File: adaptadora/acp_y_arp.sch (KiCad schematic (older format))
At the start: 39 parts, among them J12 Conn_Coaxial, J13 Conn_Coaxial, J14 Conn_Coaxial, J15 Conn_Coaxial, J16 Conn_Coaxial, J17 Conn_Coaxial, U11 LM361MX_NOPB, U12 LM361MX_NOPB, U21 TLV2772IDR, U22 TLV2772IDR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

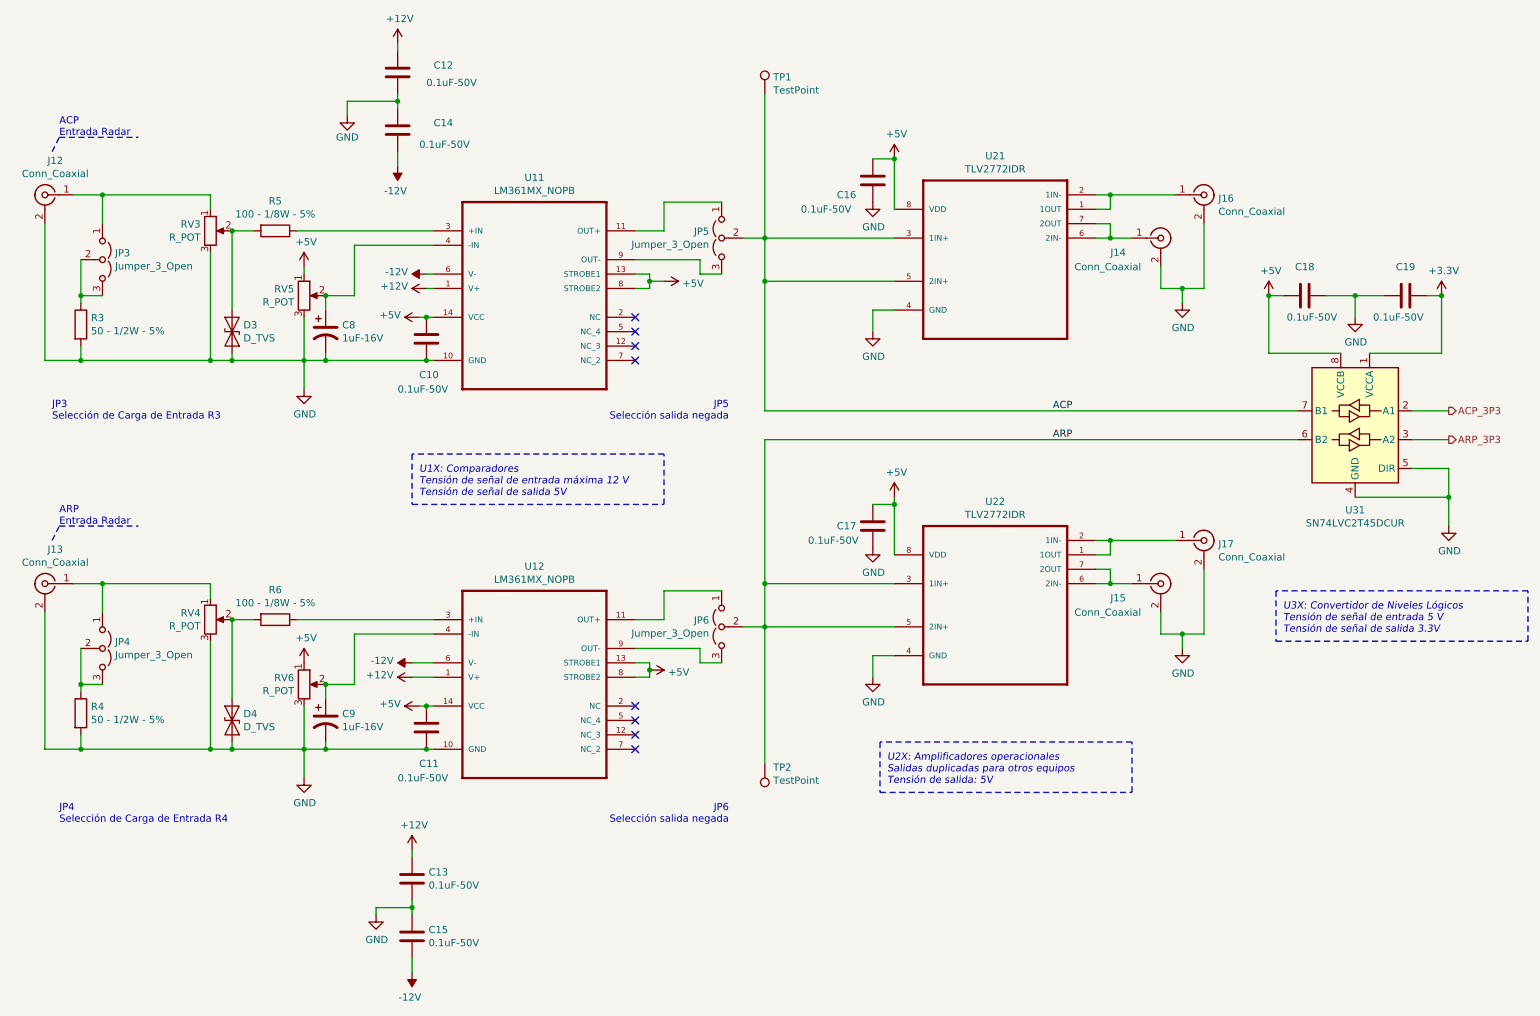
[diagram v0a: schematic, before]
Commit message: se ordenan campos de integrados
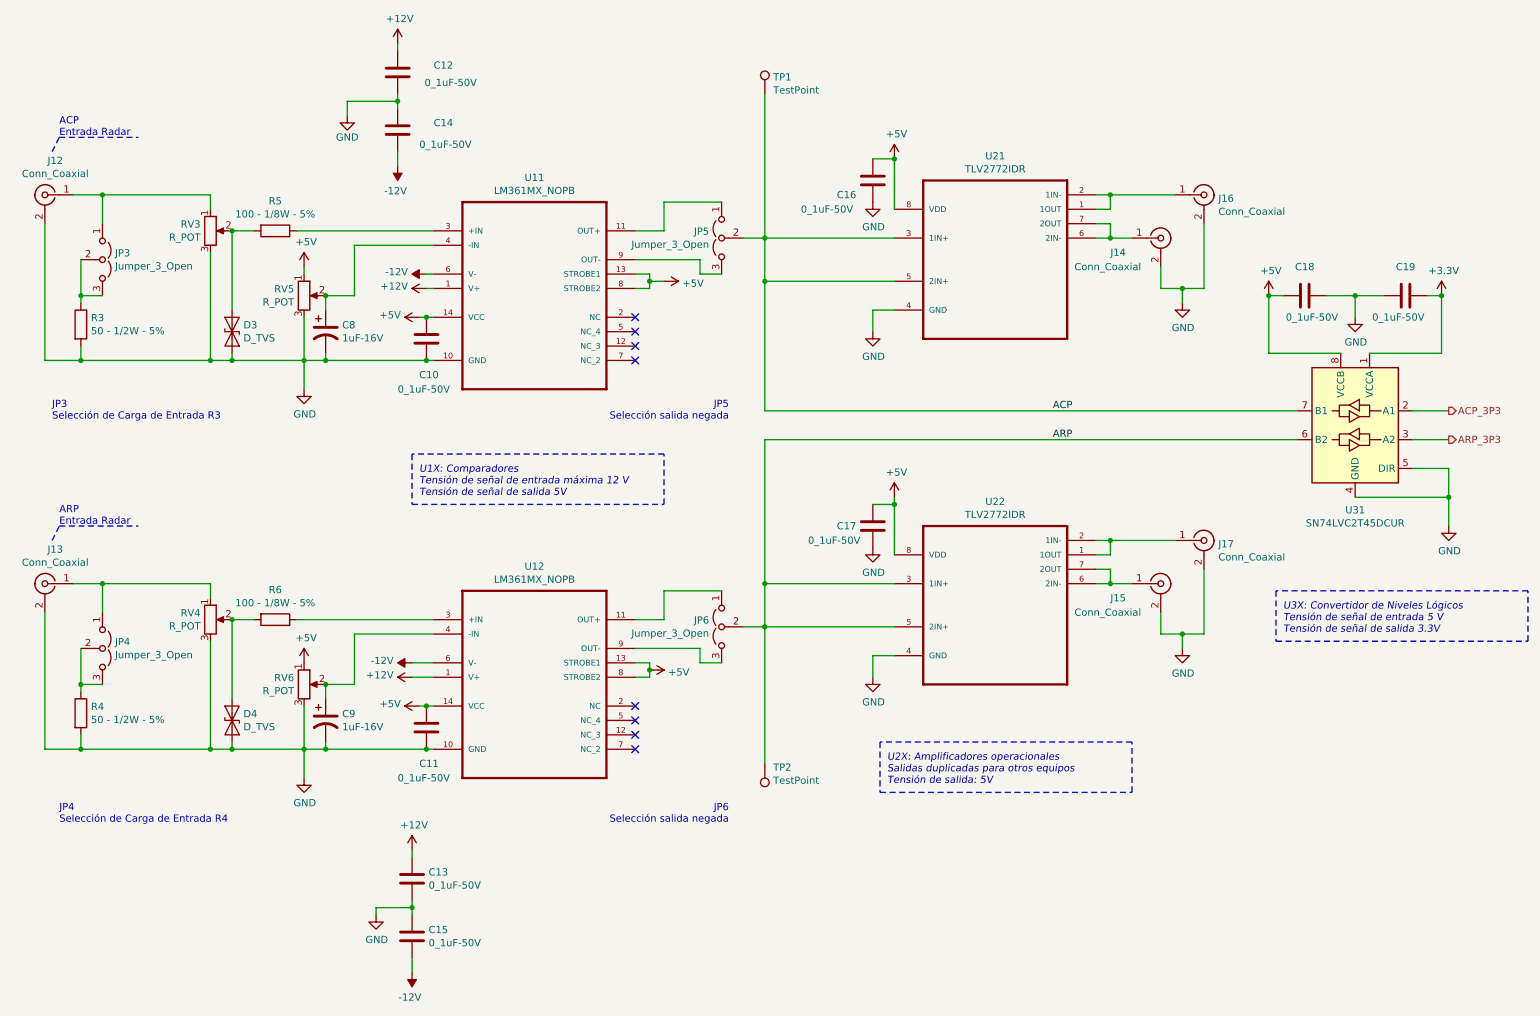
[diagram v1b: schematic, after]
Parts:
- C10, C11, C12, C13, C14, C15, C16, C17, C18, C19: value 0.1uF-50V -> 0_1uF-50V
- U11, U12: Número de parte (Digi-Key) 296-47682-1-ND -> (none)
- U21, U22: Descripción (inglés) General Purpose Amplifier 2 Circuit Rail-to-Rail 8-SOIC -> Dual 2.7-V High Slew Rate Rail-To-Rail Output Operational A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; Número de parte (Digi-Key) 296-1902-2-ND -> (none)
- U31: Número de parte (Digi-Key) 296-17014-1-ND -> (none)
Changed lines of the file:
@@
 P 3350 2950
 F 0 "C10" H 3400 3200 50  0000 R CNN
-F 1 "0.1uF-50V" H 3550 3300 50  0000 R CNN
+F 1 "0_1uF-50V" H 3550 3300 50  0000 R CNN
 F 2 "Capacitor_SMD:C_0805_2012Metric" H 3388 2800 50  0001 C CNN
 F 3 "~" H 3350 2950 50  0001 C CNN
@@
 F 4 "Texas Instruments" H 4100 2500 50  0001 L BNN "Fabricante"
 F 5 "High Speed Differential Comparator 14-SOIC 0 to 70" H 4100 2500 50  0001 L BNN "Descripción (inglés)"
-F 6 "296-47682-1-ND" H 4100 2500 50  0001 L BNN "Número de parte (Digi-Key)"
+F 6 "296-47682-1-ND" H 4100 2500 50  0001 L BNN "Número de Parte (Digi-Key)"
 F 7 "https://www.digikey.com/product-detail/en/texas-instruments/LM361MX-NOPB/296-47682-1-ND/3526971" H 4100 2500 50  0001 L BNN "Enlace"
-F 8 "296-47682-1-ND" H 4100 2500 50  0001 C CNN "Número de Parte (Digi-Key)"
 	1    4100 2500
 	1    0    0    -1
@@
 P 3150 1100
 F 0 "C12" H 2900 1150 50  0000 R CNN
-F 1 "0.1uF-50V" H 2600 1000 50  0000 L BNN
+F 1 "0_1uF-50V" H 2600 1000 50  0000 L BNN
 F 2 "Capacitor_SMD:C_0805_2012Metric" H 3188 950 50  0001 C CNN
 F 3 "~" H 3150 1100 50  0001 C CNN
@@
 P 3150 1500
 F 0 "C14" H 3400 1550 50  0000 L CNN
-F 1 "0.1uF-50V" H 3300 1400 50  0000 L CNN
+F 1 "0_1uF-50V" H 3300 1400 50  0000 L CNN
 F 2 "Capacitor_SMD:C_0805_2012Metric" H 3188 1350 50  0001 C CNN
 F 3 "~" H 3150 1500 50  0001 C CNN
@@
 F 3 "http://www.ti.com/lit/ds/symlink/tlv2772.pdf" H 7300 2250 50  0001 L BNN
 F 4 "Texas Instruments" H 7300 2250 50  0001 L BNN "Fabricante"
-F 5 "General Purpose Amplifier 2 Circuit Rail-to-Rail 8-SOIC" H 7300 2250 50  0001 L BNN "Descripción (inglés)"
+F 5 "Dual 2.7-V High Slew Rate Rail-To-Rail Output Operational Amplifier 8-SOIC -40 to 125" H 7300 2250 50  0001 L BNN "Descripción (inglés)"
 F 6 "296-1902-2-ND" H 7300 2250 50  0001 L BNN "Número de Parte (Digi-Key)"
 F 7 "https://www.digikey.com/product-detail/en/texas-instruments/TLV2772IDR/296-1902-2-ND/374332" H 7300 2250 50  0001 L BNN "Enlace"
-F 8 "296-1902-2-ND" H 7300 2250 50  0001 C CNN "Número de parte (Digi-Key)"
 	1    7300 2250
 	1    0    0    -1
@@
 P 10150 2650
 F 0 "C19" V 9950 2650 50  0000 C CNN
-F 1 "0.1uF-50V" V 10300 2600 50  0000 C CNN
+F 1 "0_1uF-50V" V 10300 2600 50  0000 C CNN
 F 2 "Capacitor_SMD:C_0805_2012Metric" H 10188 2500 50  0001 C CNN
 F 3 "~" H 10150 2650 50  0001 C CNN
@@
 F 3 "http://www.ti.com/lit/ds/symlink/sn74lvc2t45.pdf" H 8900 3000 50  0001 C CNN
 F 4 "Dual-Bit Dual-Supply Bus Transceiver With Configurable Voltage" H 9800 3550 50  0001 C CNN "Descripción (inglés)"
-F 5 "https://www.digikey.com/product-detail/en/texas-instruments/SN74LVC2T45DCUR/296-17014-2-ND/657833" H 9800 3550 50  0001 C CNN "Enlace"
-F 6 "Texas Instruments" H 9800 3550 50  0001 C CNN "Fabricante"
-F 7 "296-17014-1-ND" H 9800 3550 50  0001 C CNN "Número de Parte (Digi-Key)"
-F 8 "296-17014-1-ND" H 9800 3550 50  0001 C CNN "Número de parte (Digi-Key)"
+F 5 "Texas Instruments" H 9800 3550 50  0001 C CNN "Fabricante"
+F 6 "296-17014-1-ND" H 9800 3550 50  0001 C CNN "Número de Parte (Digi-Key)"
+F 7 "https://www.digikey.com/product-detail/en/texas-instruments/SN74LVC2T45DCUR/296-17014-2-ND/657833" H 9800 3550 50  0001 C CNN "Enlace"
 	1    9800 3550
 	-1   0    0    -1
@@
 P 6450 1850
 F 0 "C16" H 6200 1750 50  0000 L CNN
-F 1 "0.1uF-50V" H 5950 1650 50  0000 L CNN
+F 1 "0_1uF-50V" H 5950 1650 50  0000 L CNN
 F 2 "Capacitor_SMD:C_0805_2012Metric" H 6488 1700 50  0001 C CNN
 F 3 "~" H 6450 1850 50  0001 C CNN
@@
 P 3350 5650
 F 0 "C11" H 3400 5900 50  0000 R CNN
-F 1 "0.1uF-50V" H 3550 6000 50  0000 R CNN
+F 1 "0_1uF-50V" H 3550 6000 50  0000 R CNN
 F 2 "Capacitor_SMD:C_0805_2012Metric" H 3388 5500 50  0001 C CNN
 F 3 "~" H 3350 5650 50  0001 C CNN
@@
 F 4 "Texas Instruments" H 4100 5200 50  0001 L BNN "Fabricante"
 F 5 "High Speed Differential Comparator 14-SOIC 0 to 70" H 4100 5200 50  0001 L BNN "Descripción (inglés)"
-F 6 "296-47682-1-ND" H 4100 5200 50  0001 L BNN "Número de parte (Digi-Key)"
+F 6 "296-47682-1-ND" H 4100 5200 50  0001 L BNN "Número de Parte (Digi-Key)"
 F 7 "https://www.digikey.com/product-detail/en/texas-instruments/LM361MX-NOPB/296-47682-1-ND/3526971" H 4100 5200 50  0001 L BNN "Enlace"
-F 8 "296-47682-1-ND" H 4100 5200 50  0001 C CNN "Número de Parte (Digi-Key)"
 	1    4100 5200
 	1    0    0    -1
@@
 P 3250 6700
 F 0 "C13" H 3135 6746 50  0000 R CNN
-F 1 "0.1uF-50V" H 3135 6655 50  0000 R CNN
+F 1 "0_1uF-50V" H 3135 6655 50  0000 R CNN
 F 2 "Capacitor_SMD:C_0805_2012Metric" H 3288 6550 50  0001 C CNN
 F 3 "~" H 3250 6700 50  0001 C CNN
@@
 P 3250 7100
 F 0 "C15" H 3365 7146 50  0000 L CNN
-F 1 "0.1uF-50V" H 3365 7055 50  0000 L CNN
+F 1 "0_1uF-50V" H 3365 7055 50  0000 L CNN
 F 2 "Capacitor_SMD:C_0805_2012Metric" H 3288 6950 50  0001 C CNN
 F 3 "~" H 3250 7100 50  0001 C CNN
@@
 F 3 "http://www.ti.com/lit/ds/symlink/tlv2772.pdf" H 7300 4650 50  0001 L BNN
 F 4 "Texas Instruments" H 7300 4650 50  0001 L BNN "Fabricante"
-F 5 "General Purpose Amplifier 2 Circuit Rail-to-Rail 8-SOIC" H 7300 4650 50  0001 L BNN "Descripción (inglés)"
+F 5 "Dual 2.7-V High Slew Rate Rail-To-Rail Output Operational Amplifier 8-SOIC -40 to 125" H 7300 4650 50  0001 L BNN "Descripción (inglés)"
 F 6 "296-1902-2-ND" H 7300 4650 50  0001 L BNN "Número de Parte (Digi-Key)"
 F 7 "https://www.digikey.com/product-detail/en/texas-instruments/TLV2772IDR/296-1902-2-ND/374332" H 7300 4650 50  0001 L BNN "Enlace"
-F 8 "296-1902-2-ND" H 7300 4650 50  0001 C CNN "Número de parte (Digi-Key)"
 	1    7300 4650
 	1    0    0    -1
@@
 P 6450 4250
 F 0 "C17" H 6200 4250 50  0000 L CNN
-F 1 "0.1uF-50V" H 6000 4150 50  0000 L CNN
+F 1 "0_1uF-50V" H 6000 4150 50  0000 L CNN
 F 2 "Capacitor_SMD:C_0805_2012Metric" H 6488 4100 50  0001 C CNN
 F 3 "~" H 6450 4250 50  0001 C CNN
@@
 P 9450 2650
 F 0 "C18" V 9250 2650 50  0000 C CNN
-F 1 "0.1uF-50V" V 9600 2700 50  0000 C CNN
+F 1 "0_1uF-50V" V 9600 2700 50  0000 C CNN
 F 2 "Capacitor_SMD:C_0805_2012Metric" H 9488 2500 50  0001 C CNN
 F 3 "~" H 9450 2650 50  0001 C CNN

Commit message: se cambia footprint de componentes y el posicionamiento
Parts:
- D3, D4: footprint Diode_SMD:D_0201_0603Metric -> Diode_THT:D_DO-15_P10.16mm_Horizontal
- JP3, JP4, JP5, JP6: footprint Jumper:SolderJumper-3_P1.3mm_Open_Pad1.0x1.5mm_NumberLabels -> Connector_PinHeader_2.54mm:PinHeader_1x03_P2.54mm_Vertical
- U11, U12: footprint Package_SO:SOIC-14_3.9x8.7mm_P1.27mm -> Package_DIP:DIP-14_W7.62mm_Socket
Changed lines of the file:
@@
 F 0 "D3" V 1954 2979 50  0000 L CNN
 F 1 "D_TVS" V 2045 2979 50  0000 L CNN
-F 2 "Diode_SMD:D_0201_0603Metric" H 2000 2900 50  0001 C CNN
+F 2 "Diode_THT:D_DO-15_P10.16mm_Horizontal" H 2000 2900 50  0001 C CNN
 F 3 "~" H 2000 2900 50  0001 C CNN
 	1    2000 2900
@@
 F 0 "JP3" V 1054 2487 50  0000 L CNN
 F 1 "Jumper_3_Open" V 1145 2487 50  0000 L CNN
-F 2 "Jumper:SolderJumper-3_P1.3mm_Open_Pad1.0x1.5mm_NumberLabels" H 1100 2400 50  0001 C CNN
+F 2 "Connector_PinHeader_2.54mm:PinHeader_1x03_P2.54mm_Vertical" H 1100 2400 50  0001 C CNN
 F 3 "~" H 1100 2400 50  0001 C CNN
 	1    1100 2400
@@
 F 0 "U11" H 4100 3170 50  0000 C CNN
 F 1 "LM361MX_NOPB" H 4100 3079 50  0000 C CNN
-F 2 "Package_SO:SOIC-14_3.9x8.7mm_P1.27mm" H 4100 2500 50  0001 L BNN
+F 2 "Package_DIP:DIP-14_W7.62mm_Socket" H 4100 2500 50  0001 L BNN
 F 3 "http://www.ti.com/lit/ds/symlink/lm361.pdf" H 4100 2500 50  0001 L BNN
 F 4 "Texas Instruments" H 4100 2500 50  0001 L BNN "Fabricante"
@@
 F 0 "JP5" V 5354 2337 50  0000 L CNN
 F 1 "Jumper_3_Open" V 5445 2337 50  0000 L CNN
-F 2 "Jumper:SolderJumper-3_P1.3mm_Open_Pad1.0x1.5mm_NumberLabels" H 5400 2250 50  0001 C CNN
+F 2 "Connector_PinHeader_2.54mm:PinHeader_1x03_P2.54mm_Vertical" H 5400 2250 50  0001 C CNN
 F 3 "~" H 5400 2250 50  0001 C CNN
 	1    5400 2250
@@
 F 0 "D4" V 1954 5679 50  0000 L CNN
 F 1 "D_TVS" V 2045 5679 50  0000 L CNN
-F 2 "Diode_SMD:D_0201_0603Metric" H 2000 5600 50  0001 C CNN
+F 2 "Diode_THT:D_DO-15_P10.16mm_Horizontal" H 2000 5600 50  0001 C CNN
 F 3 "~" H 2000 5600 50  0001 C CNN
 	1    2000 5600
@@
 F 0 "JP4" V 1054 5187 50  0000 L CNN
 F 1 "Jumper_3_Open" V 1145 5187 50  0000 L CNN
-F 2 "Jumper:SolderJumper-3_P1.3mm_Open_Pad1.0x1.5mm_NumberLabels" H 1100 5100 50  0001 C CNN
+F 2 "Connector_PinHeader_2.54mm:PinHeader_1x03_P2.54mm_Vertical" H 1100 5100 50  0001 C CNN
 F 3 "~" H 1100 5100 50  0001 C CNN
 	1    1100 5100
@@
 F 0 "U12" H 4100 5870 50  0000 C CNN
 F 1 "LM361MX_NOPB" H 4100 5779 50  0000 C CNN
-F 2 "Package_SO:SOIC-14_3.9x8.7mm_P1.27mm" H 4100 5200 50  0001 L BNN
+F 2 "Package_DIP:DIP-14_W7.62mm_Socket" H 4100 5200 50  0001 L BNN
 F 3 "http://www.ti.com/lit/ds/symlink/lm361.pdf" H 4100 5200 50  0001 L BNN
 F 4 "Texas Instruments" H 4100 5200 50  0001 L BNN "Fabricante"
@@
 F 0 "JP6" V 5354 5037 50  0000 L CNN
 F 1 "Jumper_3_Open" V 5445 5037 50  0000 L CNN
-F 2 "Jumper:SolderJumper-3_P1.3mm_Open_Pad1.0x1.5mm_NumberLabels" H 5400 4950 50  0001 C CNN
+F 2 "Connector_PinHeader_2.54mm:PinHeader_1x03_P2.54mm_Vertical" H 5400 4950 50  0001 C CNN
 F 3 "~" H 5400 4950 50  0001 C CNN
 	1    5400 4950

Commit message: modificaciones bom
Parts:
- U11, U12: Descripción (inglés) High Speed Differential Comparator 14-SOIC 0 to 70 -> High Speed Differential Comparator; Enlace https://www.digikey.com/product-detail/en/texas-instruments/LM361MX-NOPB/296-47682-1-ND/3526971 -> https://www.digikey.com/product-detail/en/texas-instruments/LM361N-NOPB/LM361N-NOPB-ND/32491; Número de Parte (Digi-Key) 296-47682-1-ND -> LM361N/NOPB-ND
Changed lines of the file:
@@
 F 3 "http://www.ti.com/lit/ds/symlink/lm361.pdf" H 4100 2500 50  0001 L BNN
 F 4 "Texas Instruments" H 4100 2500 50  0001 L BNN "Fabricante"
-F 5 "High Speed Differential Comparator 14-SOIC 0 to 70" H 4100 2500 50  0001 L BNN "Descripción (inglés)"
-F 6 "296-47682-1-ND" H 4100 2500 50  0001 L BNN "Número de Parte (Digi-Key)"
-F 7 "https://www.digikey.com/product-detail/en/texas-instruments/LM361MX-NOPB/296-47682-1-ND/3526971" H 4100 2500 50  0001 L BNN "Enlace"
+F 5 "High Speed Differential Comparator" H 4100 2500 50  0001 L BNN "Descripción (inglés)"
+F 6 "LM361N/NOPB-ND" H 4100 2500 50  0001 L BNN "Número de Parte (Digi-Key)"
+F 7 "https://www.digikey.com/product-detail/en/texas-instruments/LM361N-NOPB/LM361N-NOPB-ND/32491" H 4100 2500 50  0001 L BNN "Enlace"
 	1    4100 2500
 	1    0    0    -1
@@
 F 3 "http://www.ti.com/lit/ds/symlink/lm361.pdf" H 4100 5200 50  0001 L BNN
 F 4 "Texas Instruments" H 4100 5200 50  0001 L BNN "Fabricante"
-F 5 "High Speed Differential Comparator 14-SOIC 0 to 70" H 4100 5200 50  0001 L BNN "Descripción (inglés)"
-F 6 "296-47682-1-ND" H 4100 5200 50  0001 L BNN "Número de Parte (Digi-Key)"
-F 7 "https://www.digikey.com/product-detail/en/texas-instruments/LM361MX-NOPB/296-47682-1-ND/3526971" H 4100 5200 50  0001 L BNN "Enlace"
+F 5 "High Speed Differential Comparator" H 4100 5200 50  0001 L BNN "Descripción (inglés)"
+F 6 "LM361N/NOPB-ND" H 4100 5200 50  0001 L BNN "Número de Parte (Digi-Key)"
+F 7 "https://www.digikey.com/product-detail/en/texas-instruments/LM361N-NOPB/LM361N-NOPB-ND/32491" H 4100 5200 50  0001 L BNN "Enlace"
 	1    4100 5200
 	1    0    0    -1
